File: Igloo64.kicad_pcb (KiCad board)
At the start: 2 copper layers, 96.5 x 90.2 mm, 10 parts, among them J1 Conn_02x32_Counter_Clockwise, J10 Conn_01x32, J2 Conn_02x16_Odd_Even, J3 Conn_02x16_Odd_Even, J4 Conn_02x16_Odd_Even, J5 Conn_02x16_Odd_Even, J6 Conn_02x32_Odd_Even, J7 Conn_02x32_Odd_Even, J8 Conn_02x32_Odd_Even, J9 Conn_01x32

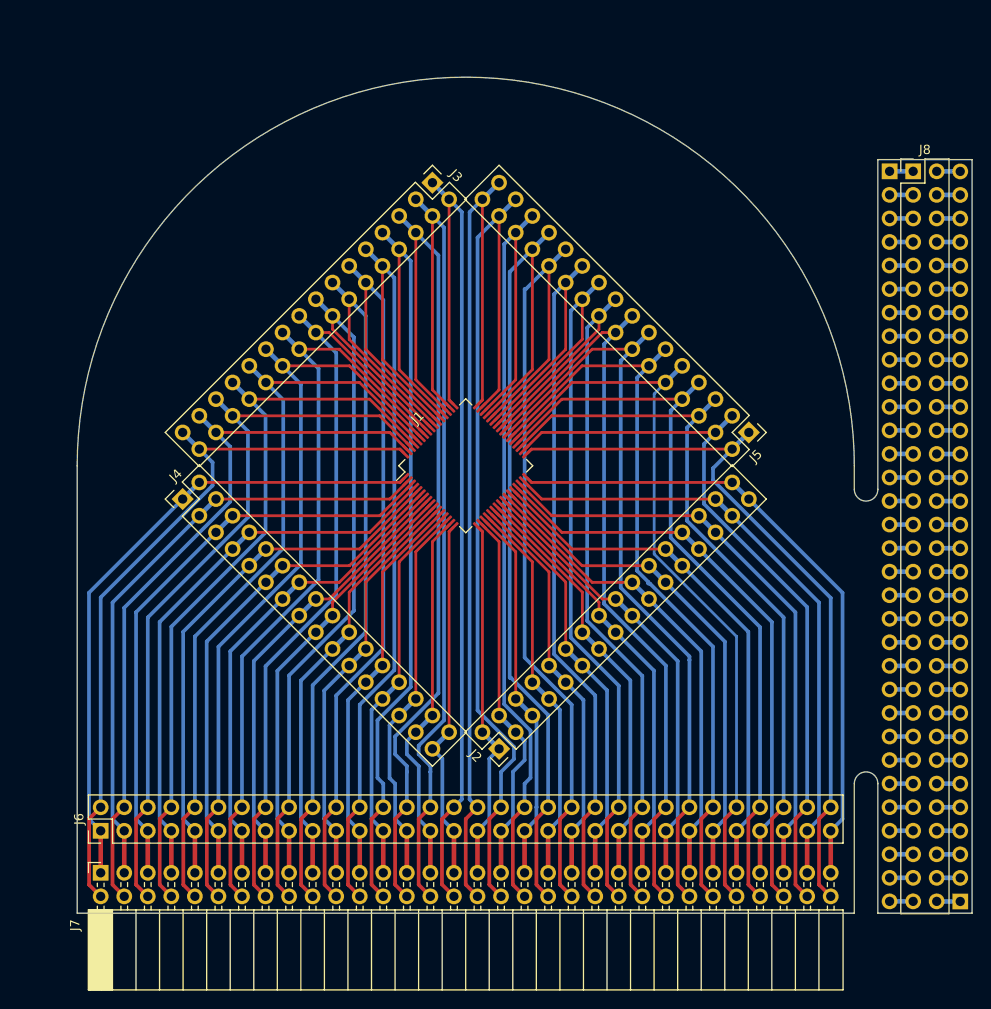
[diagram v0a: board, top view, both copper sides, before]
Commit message: Add nine big LEDs.
Place nine 10mm LEDs around the curved upper edge of the PCB. There's just enough room for the LEDs and the two-pin headers to connect them up. Also fix the width of one track that was too narrow.
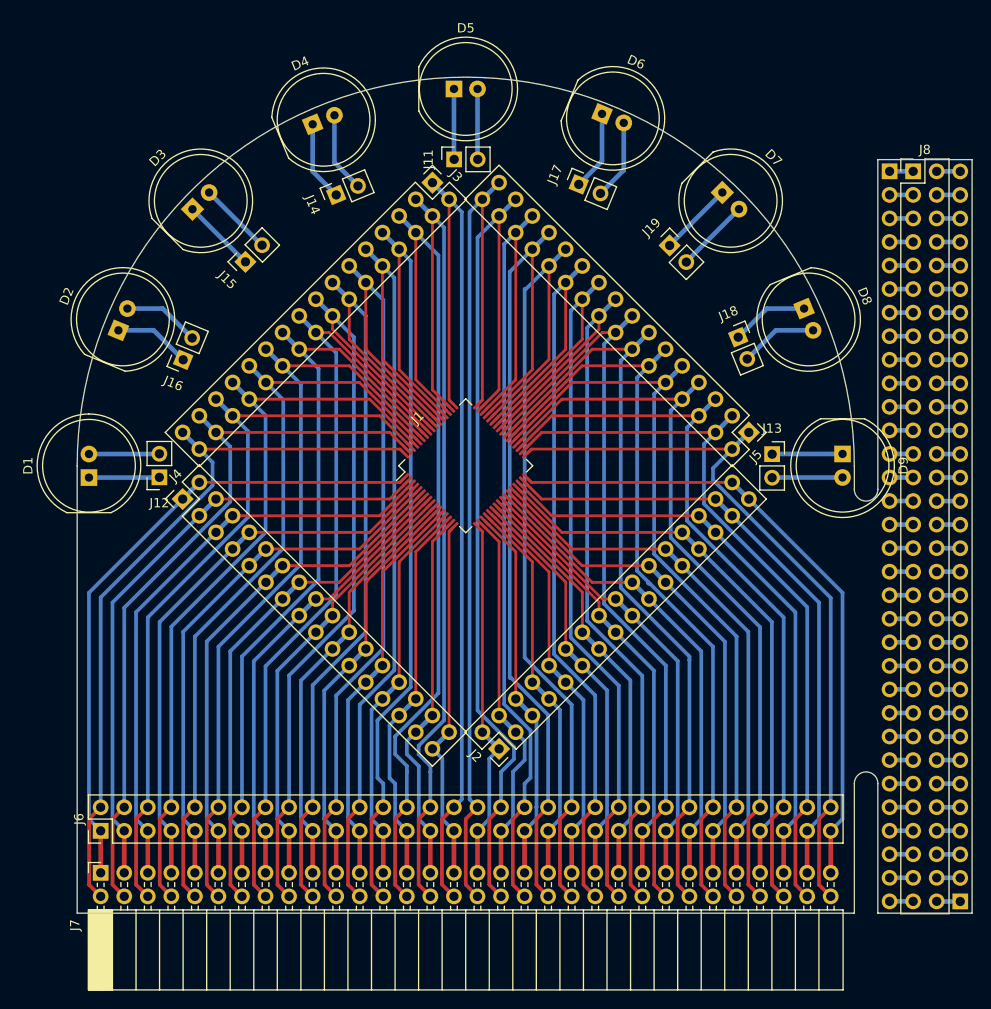
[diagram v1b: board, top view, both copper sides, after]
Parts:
- added D1: LED, LED_THT:LED_D10.0mm, F.Cu at (91.4, 90.2)
- added D2: LED, LED_THT:LED_D10.0mm, F.Cu at (94.6, 74.3)
- added D3: LED, LED_THT:LED_D10.0mm, F.Cu at (102.6, 61.2)
- added D4: LED, LED_THT:LED_D10.0mm, F.Cu at (115.6, 52.1)
- added D5: LED, LED_THT:LED_D10.0mm, F.Cu at (130.8, 48.3)
- added D6: LED, LED_THT:LED_D10.0mm, F.Cu at (146.8, 50.9)
- added D7: LED, LED_THT:LED_D10.0mm, F.Cu at (159.8, 59.4)
- added D8: LED, LED_THT:LED_D10.0mm, F.Cu at (168.6, 71.9)
- added D9: LED, LED_THT:LED_D10.0mm, F.Cu at (172.7, 87.6)
- added J11: Conn_01x02, Connector_PinSocket_2.54mm:PinSocket_1x02_P2.54mm_Vertical, F.Cu at (130.8, 55.9)
- added J12: Conn_01x02, Connector_PinSocket_2.54mm:PinSocket_1x02_P2.54mm_Vertical, F.Cu at (99.0, 90.2)
- added J13: Conn_01x02, Connector_PinSocket_2.54mm:PinSocket_1x02_P2.54mm_Vertical, F.Cu at (165.1, 87.7)
- added J14: Conn_01x02, Connector_PinSocket_2.54mm:PinSocket_1x02_P2.54mm_Vertical, F.Cu at (118.1, 59.7)
- added J15: Conn_01x02, Connector_PinSocket_2.54mm:PinSocket_1x02_P2.54mm_Vertical, F.Cu at (108.3, 66.9)
- added J16: Conn_01x02, Connector_PinSocket_2.54mm:PinSocket_1x02_P2.54mm_Vertical, F.Cu at (101.6, 77.5)
- added J17: Conn_01x02, Connector_PinSocket_2.54mm:PinSocket_1x02_P2.54mm_Vertical, F.Cu at (144.3, 58.6)
- added J18: Conn_01x02, Connector_PinSocket_2.54mm:PinSocket_1x02_P2.54mm_Vertical, F.Cu at (161.5, 75.0)
- added J19: Conn_01x02, Connector_PinSocket_2.54mm:PinSocket_1x02_P2.54mm_Vertical, F.Cu at (154.1, 65.1)
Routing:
- net Net-(D4-Pad2): track 0.00 -> 8.67 mm
- net Net-(D4-Pad1): track 0.00 -> 8.67 mm
- net Net-(D6-Pad2): track 0.00 -> 8.65 mm
- net Net-(D6-Pad1): track 0.00 -> 8.65 mm
- net Net-(D8-Pad2): track 0.00 -> 8.38 mm
- net Net-(D8-Pad1): track 0.00 -> 8.38 mm
- net Net-(D2-Pad1): track 0.00 -> 8.30 mm
- net Net-(D2-Pad2): track 0.00 -> 8.30 mm
- net Net-(D3-Pad2): track 0.00 -> 8.07 mm
- net Net-(D3-Pad1): track 0.00 -> 8.07 mm
- net Net-(D7-Pad2): track 0.00 -> 8.07 mm
- net Net-(D7-Pad1): track 0.00 -> 8.07 mm
- net Net-(D1-Pad2): track 0.00 -> 7.61 mm
- net Net-(D9-Pad1): track 0.00 -> 7.61 mm
- net Net-(D1-Pad1): track 0.00 -> 7.61 mm
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
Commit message: Renumber LED connectors.
Also remove unconnected track on /pin49.
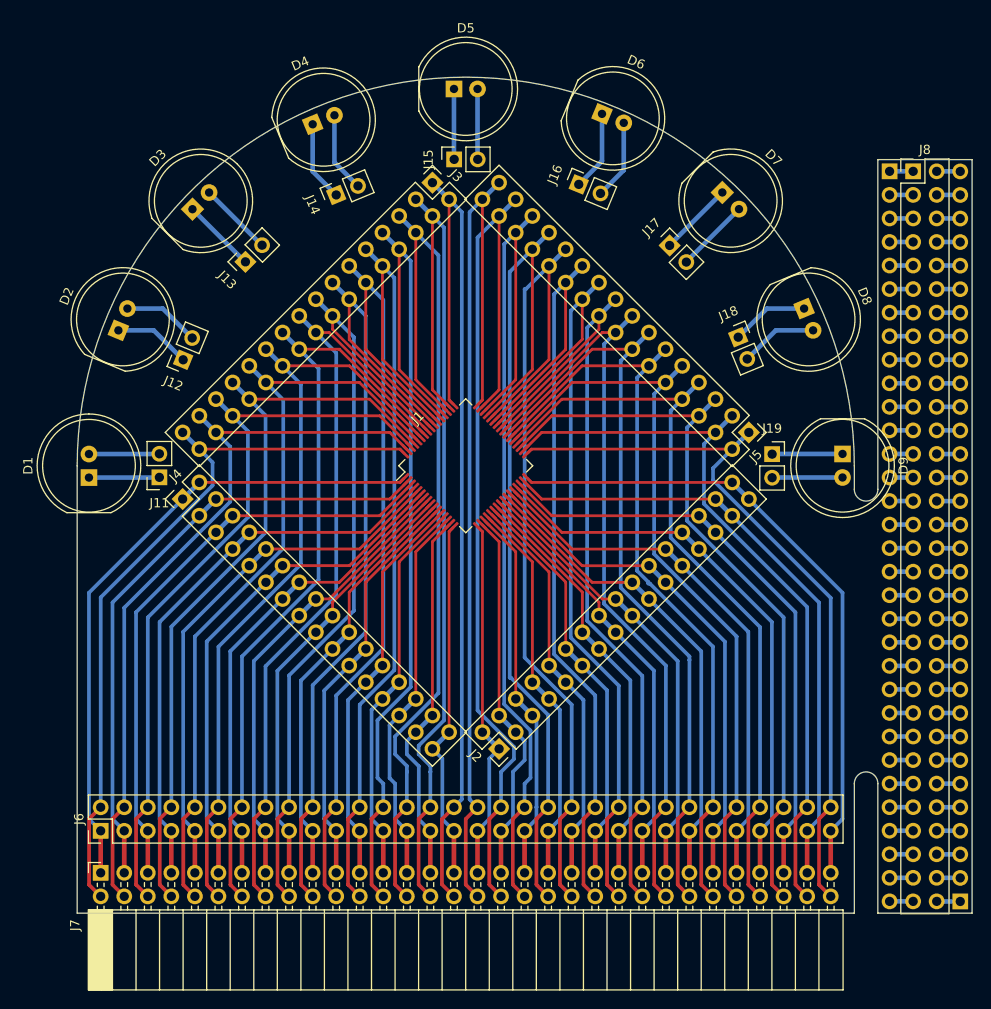
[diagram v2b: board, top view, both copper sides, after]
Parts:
- renumbered J12 to J11, J16 to J12, J15 to J13, J11 to J15, J17 to J16, J19 to J17, J13 to J19
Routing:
- net /pin49: track 102.5 -> 102.0 mm
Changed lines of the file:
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@@
   (net 63 "/pin38")
   (net 64 "/pin37")
-  (net 65 "Net-(J11-Pad1)")
+  (net 65 "Net-(D5-Pad1)")
   (net 66 "Net-(J10-Pad32)")
-  (net 67 "Net-(J11-Pad2)")
+  (net 67 "Net-(D5-Pad2)")
   (net 68 "Net-(J10-Pad31)")
   (net 69 "Net-(J8-Pad1)")
@@
     (property "Sheetname" "")
     (attr through_hole)
-    (fp_text reference "J15" (at 0 -2.77 135) (layer "F.SilkS")
+    (fp_text reference "J13" (at 0 -2.77 135) (layer "F.SilkS")
       (effects (font (size 1 1) (thickness 0.15)))
     )
@@
     (fp_circle (center 1.27 0) (end 6.27 0) (layer "F.Fab") (width 0.1) (fill none))
     (pad "1" thru_hole rect (at 0 0) (size 1.8 1.8) (drill 0.9) (layers *.Cu *.Mask)
-      (net 65 "Net-(J11-Pad1)") (pinfunction "K") (pintype "passive"))
+      (net 65 "Net-(D5-Pad1)") (pinfunction "K") (pintype "passive"))
     (pad "2" thru_hole circle (at 2.54 0) (size 1.8 1.8) (drill 0.9) (layers *.Cu *.Mask)
-      (net 67 "Net-(J11-Pad2)") (pinfunction "A") (pintype "passive"))
+      (net 67 "Net-(D5-Pad2)") (pinfunction "A") (pintype "passive"))
     (model "${KICAD6_3DMODEL_DIR}/LED_THT.3dshapes/LED_D10.0mm.wrl"
       (offset (xyz 0 0 0))
@@
     (property "Sheetname" "")
     (attr through_hole)
-    (fp_text reference "J16" (at 0 -2.77 157.5) (layer "F.SilkS")
+    (fp_text reference "J12" (at 0 -2.77 157.5) (layer "F.SilkS")
       (effects (font (size 1 1) (thickness 0.15)))
     )
@@
     (property "Sheetname" "")
     (attr through_hole)
-    (fp_text reference "J19" (at 0 -2.77 45) (layer "F.SilkS")
+    (fp_text reference "J17" (at 0 -2.77 45) (layer "F.SilkS")
       (effects (font (size 1 1) (thickness 0.15)))
     )
@@
     (property "Sheetname" "")
     (attr through_hole)
-    (fp_text reference "J11" (at 0 -2.77 90) (layer "F.SilkS")
+    (fp_text reference "J15" (at 0 -2.77 90) (layer "F.SilkS")
       (effects (font (size 1 1) (thickness 0.15)))
     )
@@
     (fp_line (start 1.27 3.81) (end -1.27 3.81) (layer "F.Fab") (width 0.1))
     (pad "1" thru_hole rect (at 0 0 90) (size 1.7 1.7) (drill 1) (layers *.Cu *.Mask)
-      (net 65 "Net-(J11-Pad1)") (pinfunction "Pin_1") (pintype "passive"))
+      (net 65 "Net-(D5-Pad1)") (pinfunction "Pin_1") (pintype "passive"))
     (pad "2" thru_hole oval (at 0 2.54 90) (size 1.7 1.7) (drill 1) (layers *.Cu *.Mask)
-      (net 67 "Net-(J11-Pad2)") (pinfunction "Pin_2") (pintype "passive"))
+      (net 67 "Net-(D5-Pad2)") (pinfunction "Pin_2") (pintype "passive"))
     (model "${KICAD6_3DMODEL_DIR}/Connector_PinSocket_2.54mm.3dshapes/PinSocket_1x02_P2.54mm_Vertical.wrl"
       (offset (xyz 0 0 0))
@@
     (property "Sheetname" "")
     (attr through_hole)
-    (fp_text reference "J13" (at 0 -2.77) (layer "F.SilkS")
+    (fp_text reference "J19" (at 0 -2.77) (layer "F.SilkS")
       (effects (font (size 1 1) (thickness 0.15)))
     )
@@
     (property "Sheetname" "")
     (attr through_hole)
-    (fp_text reference "J17" (at 0 -2.77 67.5) (layer "F.SilkS")
+    (fp_text reference "J16" (at 0 -2.77 67.5) (layer "F.SilkS")
       (effects (font (size 1 1) (thickness 0.15)))
     )
@@
     (property "Sheetname" "")
     (attr through_hole)
-    (fp_text reference "J12" (at 0 -2.77) (layer "F.SilkS")
+    (fp_text reference "J11" (at 0 -2.77) (layer "F.SilkS")
       (effects (font (size 1 1) (thickness 0.15)))
     )
@@
   (segment (start 135.672102 58.367129) (end 133.876051 60.16318) (width 0.5) (layer "B.Cu") (net 9))
   (segment (start 132.495 61.544232) (end 133.876051 60.163181) (width 0.4) (layer "B.Cu") (net 9))
+  (segment (start 130.727658 82.244357) (end 130.283949 81.800648) (width 0.3) (layer "F.Cu") (net 10))
+  (segment (start 130.805 135.345) (end 129.514511 134.054511) (width 0.4) (layer "F.Cu") (net 10))
+  (segment (start 130.283949 81.800648) (end 130.283949 60.16318) (width 0.3) (layer "F.Cu") (net 10))
   (segment (start 130.805 125.735) (end 129.514511 127.025489) (width 0.4) (layer "F.Cu") (net 10))
-  (segment (start 130.727658 82.244357) (end 130.283949 81.800648) (width 0.3) (layer "F.Cu") (net 10))
-  (segment (start 130.283949 81.800648) (end 130.283949 60.16318) (width 0.3) (layer "F.Cu") (net 10))
   (segment (start 129.514511 127.025489) (end 129.514511 134.054511) (width 0.4) (layer "F.Cu") (net 10))
-  (segment (start 129.514511 134.054511) (end 130.805 135.345) (width 0.4) (layer "F.Cu") (net 10))
   (segment (start 131.655 124.885) (end 131.655 61.534231) (width 0.4) (layer "B.Cu") (net 10))
   (segment (start 130.805 125.735) (end 131.655 124.885) (width 0.4) (layer "B.Cu") (net 10))
   (segment (start 128.487898 58.367129) (end 130.283949 60.16318) (width 0.5) (layer "B.Cu") (net 10))
   (segment (start 131.655 61.534231) (end 130.283949 60.16318) (width 0.4) (layer "B.Cu") (net 10))
-  (segment (start 131.355 135.345) (end 130.805 135.345) (width 0.4) (layer "B.Cu") (net 10))
   (segment (start 114.315489 126.984511) (end 114.315489 134.095489) (width 0.4) (layer "F.Cu") (net 11))
   (segment (start 115.565 125.735) (end 114.315489 126.984511) (width 0.4) (layer "F.Cu") (net 11))
